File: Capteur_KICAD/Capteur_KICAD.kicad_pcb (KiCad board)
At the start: 2 copper layers, 68.6 x 53.3 mm, 20 parts, among them J1 Power, J2 Digital/PWM, J3 Analog, J4 Digital/PWM

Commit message: Updating PCB, proposition of final PCB
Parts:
- added C1: 100n, Capacitor_THT:C_Disc_D4.3mm_W1.9mm_P5.00mm, F.Cu at (111.0, 92.1)
- added C2: 100n, Capacitor_THT:C_Disc_D4.3mm_W1.9mm_P5.00mm, F.Cu at (143.0, 93.0)
- added C3: 100n, Capacitor_THT:C_Disc_D4.3mm_W1.9mm_P5.00mm, F.Cu at (138.0, 84.6)
- added C4: 1u, Capacitor_THT:C_Rect_L7.0mm_W4.5mm_P5.00mm, F.Cu at (121.5, 76.5)
- added C5: 100n, Capacitor_THT:C_Disc_D4.3mm_W1.9mm_P5.00mm, F.Cu at (159.5, 53.0)
- added R7: 1k, Resistor_THT:R_Axial_DIN0204_L3.6mm_D1.6mm_P5.08mm_Horizontal, F.Cu at (153.0, 89.1)
- R1, R3: footprint Resistor_THT:R_Axial_DIN0204_L3.6mm_D1.6mm_P2.54mm_Vertical -> Resistor_THT:R_Axial_DIN0204_L3.6mm_D1.6mm_P5.08mm_Horizontal
- R6: footprint Resistor_THT:R_Axial_DIN0204_L3.6mm_D1.6mm_P2.54mm_Vertical -> Resistor_THT:R_Axial_DIN0207_L6.3mm_D2.5mm_P7.62mm_Horizontal
- U4: footprint Package_DIP:CERDIP-8_W7.62mm_SideBrazed_LongPads -> LTC1050ACN8_PBF:PDIP-8_N
- moved R5 155.5 mm to (108.5, 81.6)
- moved R1 146.7 mm to (117.0, 86.9), turned to -90 degrees
- moved R3 143.1 mm to (121.5, 72.0)
- moved R6 131.6 mm to (132.2, 89.0)
- moved U6 112.9 mm to (114.7, 63.8)
- moved U8 104.2 mm to (146.5, 59.0), turned to 90 degrees
- moved U2 12.7 mm to (157.5, 92.0)
- moved U4 8.77 mm to (128.8, 89.4)
- moved U1 4.47 mm to (148.5, 56.5)
- moved U5 4.30 mm to (163.5, 85.0)
- moved U7 2.55 mm to (160.5, 57.0)
- moved U3 1.39 mm to (104.0, 83.1)
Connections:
- J3 pad 3: /A2 -> A2
- J3 pad 4: A3 -> /A3
- R3 pad 2: Net-(U4-V+) -> Net-(U4-OUT)
- U2 pad 1: +5V -> Net-(U2-V+)
- U2 pad 2: A3 -> A2
- U7 pad 2: 4 -> 3
- U7 pad 3: 3 -> 4
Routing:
- net GND: track 0.00 -> 218.5 mm
- net +5V: track 0.00 -> 204.4 mm
- net 10: track 0.00 -> 38.5 mm
- net 11: track 0.00 -> 34.8 mm
- net Net-(U4-OUT): track 0.00 -> 29.3 mm
- net 13: track 0.00 -> 29.0 mm
- net Net-(U4--IN): track 0.00 -> 24.5 mm
- net 6: track 0.00 -> 20.4 mm
- net 5: track 0.00 -> 18.1 mm
- net A4: track 0.00 -> 18.0 mm
- net 4: track 0.00 -> 16.8 mm
- net A0: track 0.00 -> 16.3 mm
- net Net-(U4-+IN): track 0.00 -> 15.8 mm
- net A5: track 0.00 -> 15.3 mm
- net 3: track 0.00 -> 13.4 mm
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- added copper zone on B.Cu, net GND

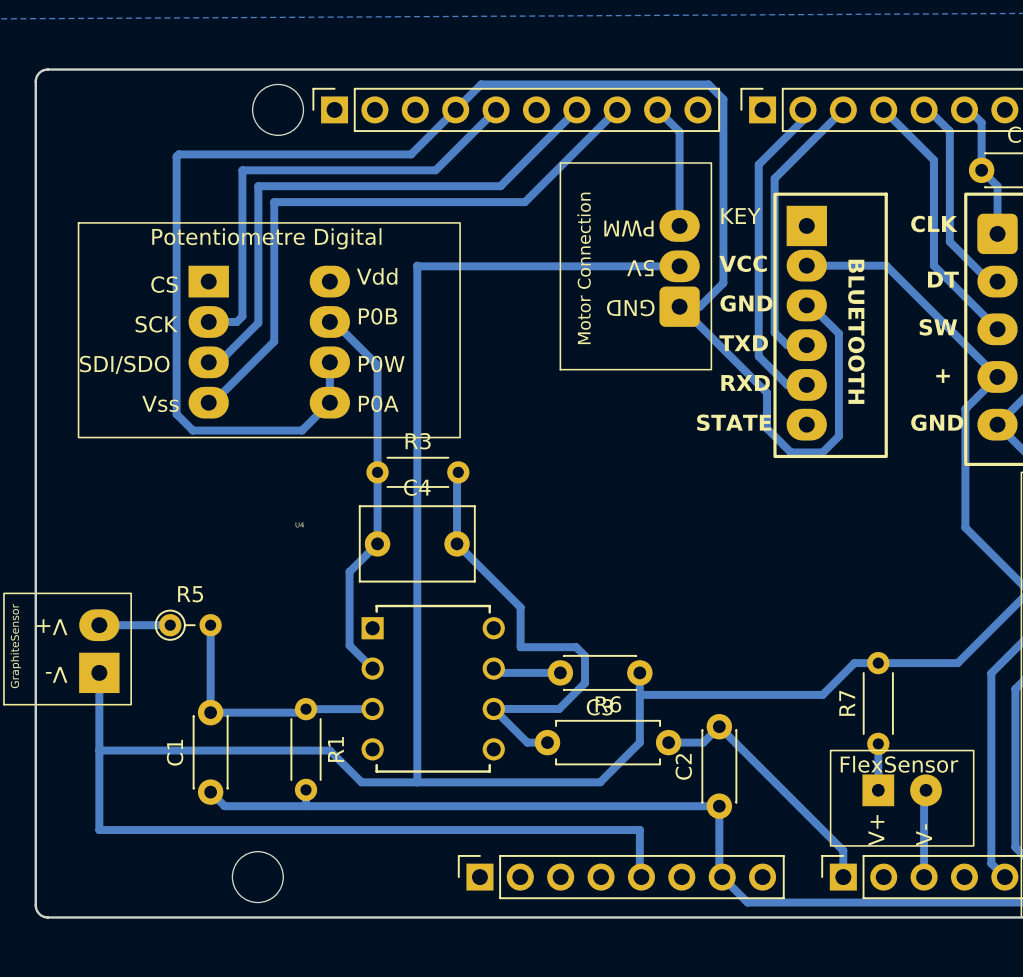
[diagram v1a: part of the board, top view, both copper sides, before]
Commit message: Updating PCB on KiCad, final proposition without 3D model
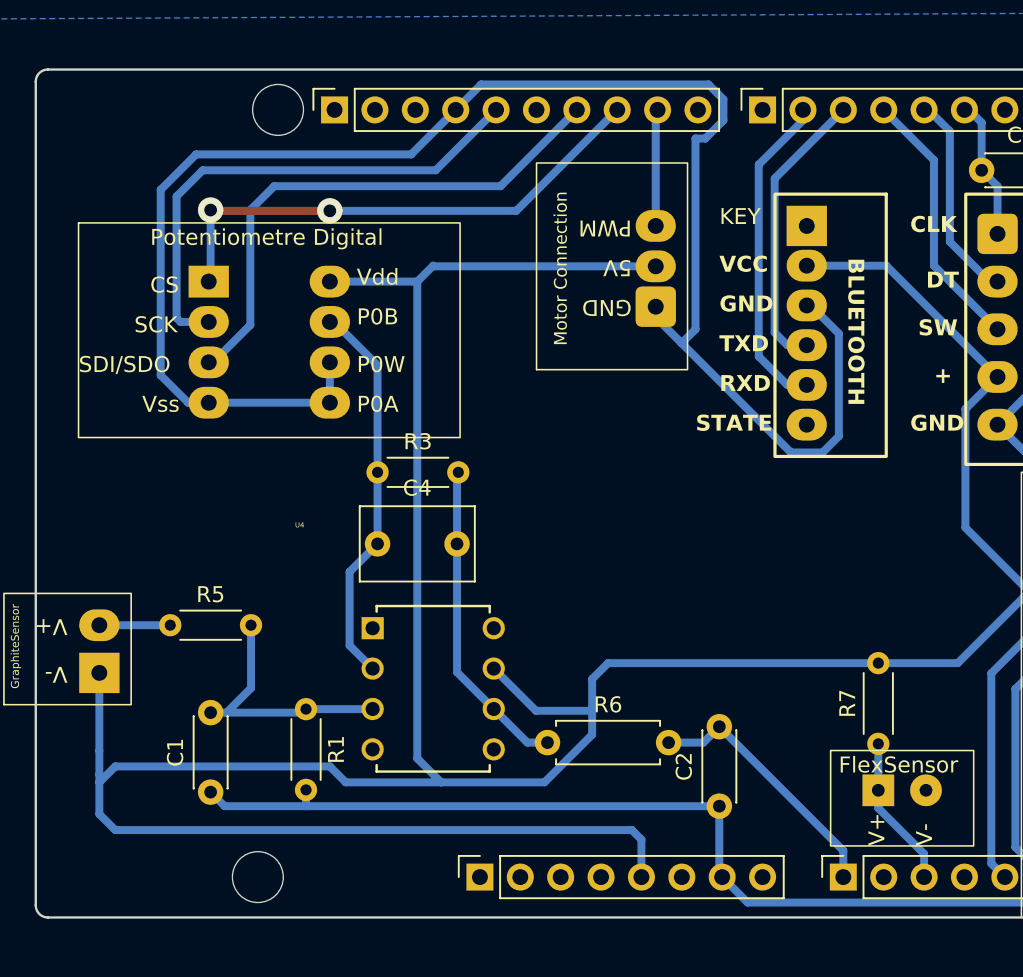
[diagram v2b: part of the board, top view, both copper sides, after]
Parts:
- removed C3: 100n, Capacitor_THT:C_Disc_D4.3mm_W1.9mm_P5.00mm
- R5: footprint Resistor_THT:R_Axial_DIN0204_L3.6mm_D1.6mm_P2.54mm_Vertical -> Resistor_THT:R_Axial_DIN0204_L3.6mm_D1.6mm_P5.08mm_Horizontal
- moved U8 1.50 mm to (145.0, 59.0)
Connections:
- R7 pad 1: Net-(U2-V+) -> A2
- U2 pad 1: Net-(U2-V+) -> A2
- U2 pad 2: A2 -> GND
- U4 pad 4: unconnected-(U4-V--Pad4) -> GND
- U4 pad 7: Net-(U4-V+) -> +5V
- U6 pad 1: unconnected-(U6-CS-Pad1) -> 10
- U6 pad 4: 10 -> GND
- U6 pad 8: unconnected-(U6-Vdd-Pad8) -> +5V
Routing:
- net +5V: track 204.4 -> 213.7 mm
- net Net-(U4-OUT): track 29.3 -> 20.1 mm
- net 10: track 38.5 -> 32.8 mm, vias 0 -> 2
- net Net-(U4-V+): track 4.30 -> 0.00 mm
- net A2: track 5.51 -> 9.57 mm
- net 13: track 29.0 -> 32.1 mm
- net Net-(U2-V+): track 2.92 -> 0.00 mm
- net Net-(U4-+IN): track 15.8 -> 16.4 mm
- net 9: track 7.87 -> 7.35 mm

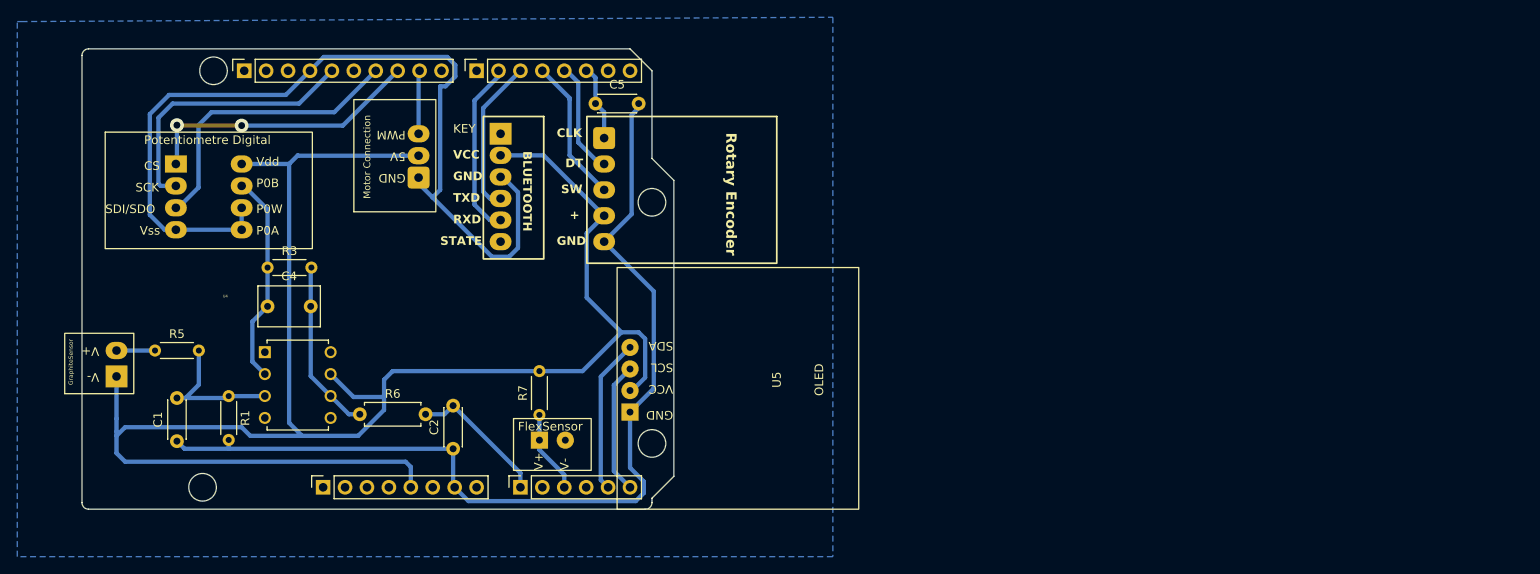
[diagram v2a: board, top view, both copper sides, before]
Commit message: Updating PCB, adding 3D models and correcting minor error on routing
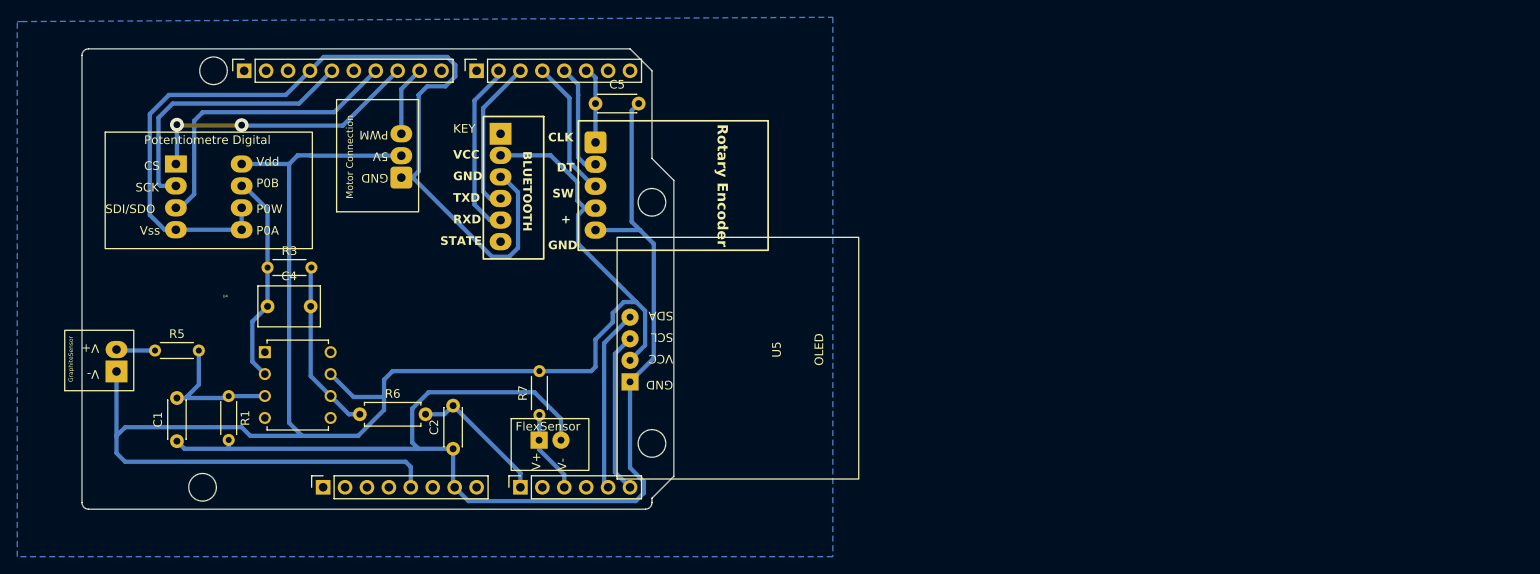
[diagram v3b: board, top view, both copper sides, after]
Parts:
- moved U5 3.50 mm to (163.5, 81.5)
- moved U2 3.27 mm to (154.2, 92.0)
- moved U8 2.00 mm to (143.0, 59.0)
- moved U7 1.12 mm to (159.5, 57.5)
- moved U3 0.34 mm to (104.0, 82.8)
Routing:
- net GND: track 219.0 -> 250.5 mm
- net A5: track 15.3 -> 18.7 mm
- net A4: track 18.0 -> 21.1 mm
- net +5V: track 213.7 -> 215.6 mm
- net 9: track 7.35 -> 8.52 mm
- net 11: track 34.7 -> 35.5 mm

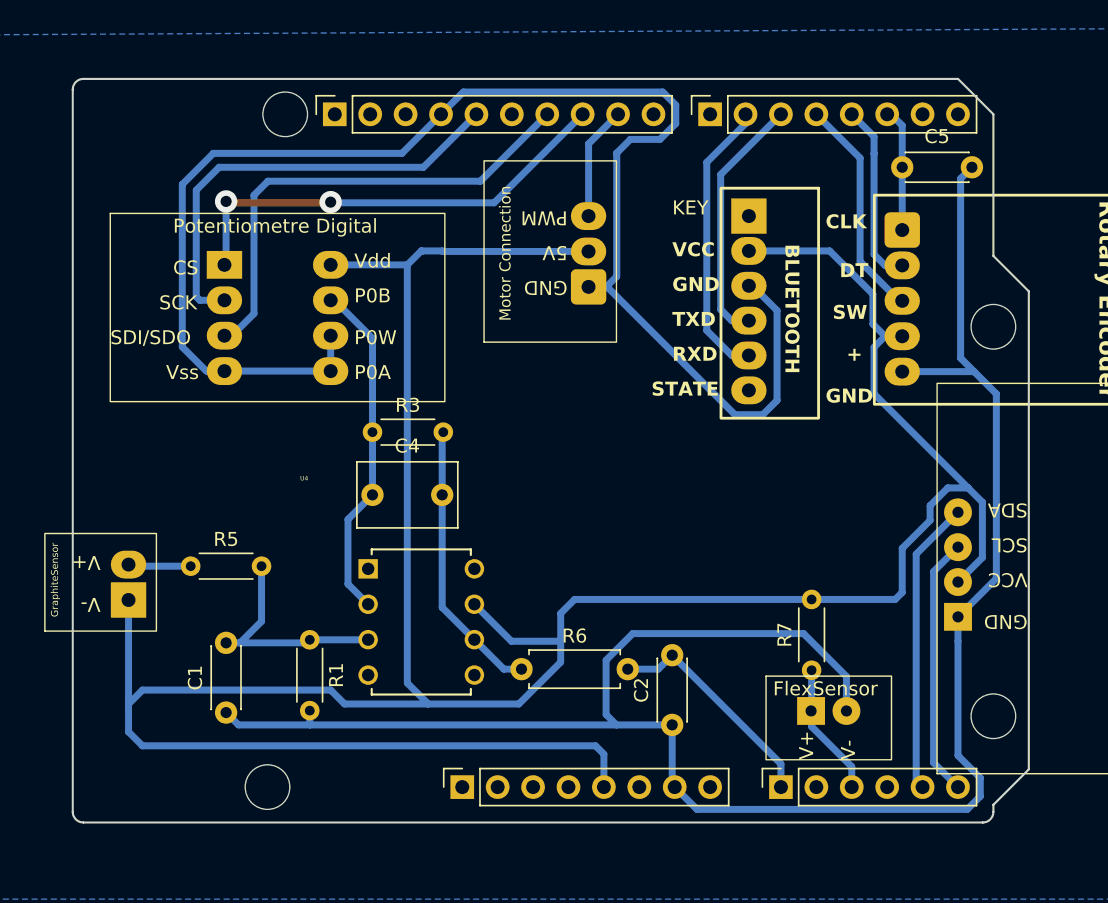
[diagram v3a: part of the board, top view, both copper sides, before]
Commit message: Pin shape correction
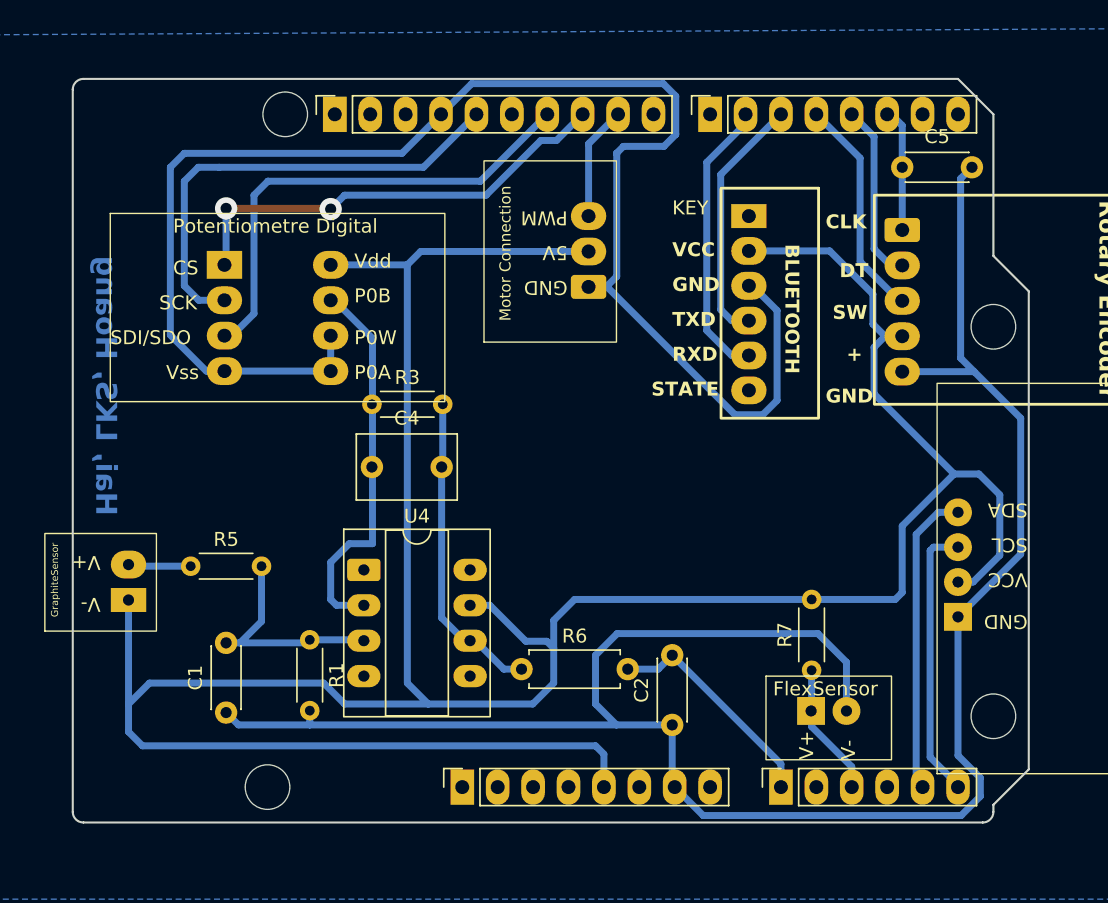
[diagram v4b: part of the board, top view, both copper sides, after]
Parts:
- U4: footprint LTC1050ACN8_PBF:PDIP-8_N -> Package_DIP:CERDIP-8_W7.62mm_SideBrazed_LongPads_Socket
- moved U4 10.9 mm to (120.9, 81.9)
- moved C4 2.00 mm to (121.5, 74.5)
- moved R3 2.00 mm to (121.5, 70.0)
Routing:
- net GND: track 250.5 -> 257.4 mm
- net +5V: track 215.6 -> 219.0 mm
- net Net-(U4--IN): track 24.5 -> 27.6 mm
- net Net-(U4-OUT): track 20.1 -> 22.6 mm
- net 13: track 32.1 -> 33.8 mm
- net A5: track 18.7 -> 19.9 mm
- net A4: track 21.1 -> 22.0 mm
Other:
- board text added: "Hai, LKS, Hoang"
